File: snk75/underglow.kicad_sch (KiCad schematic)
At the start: 48 parts

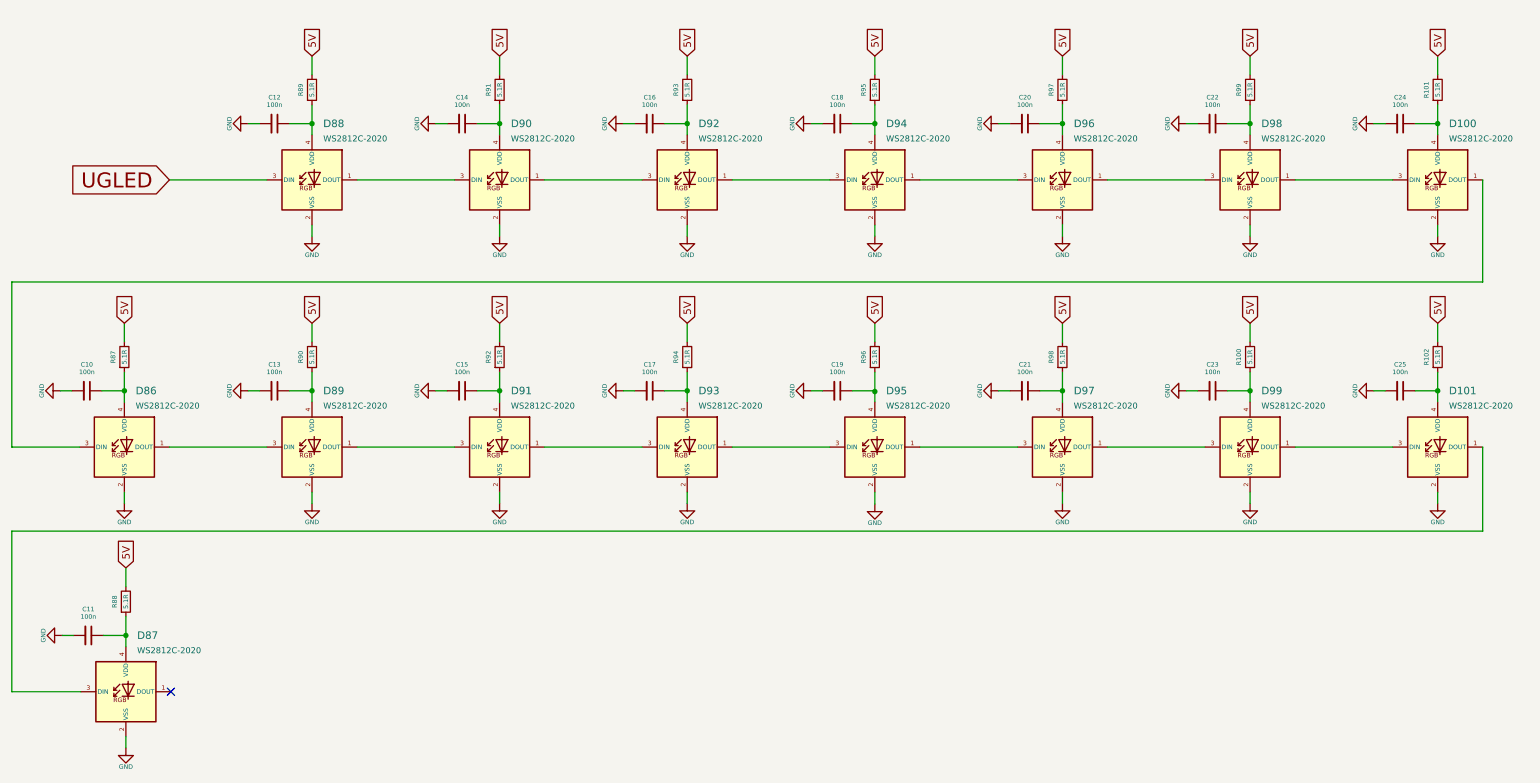
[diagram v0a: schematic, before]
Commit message: added components on board and began routing
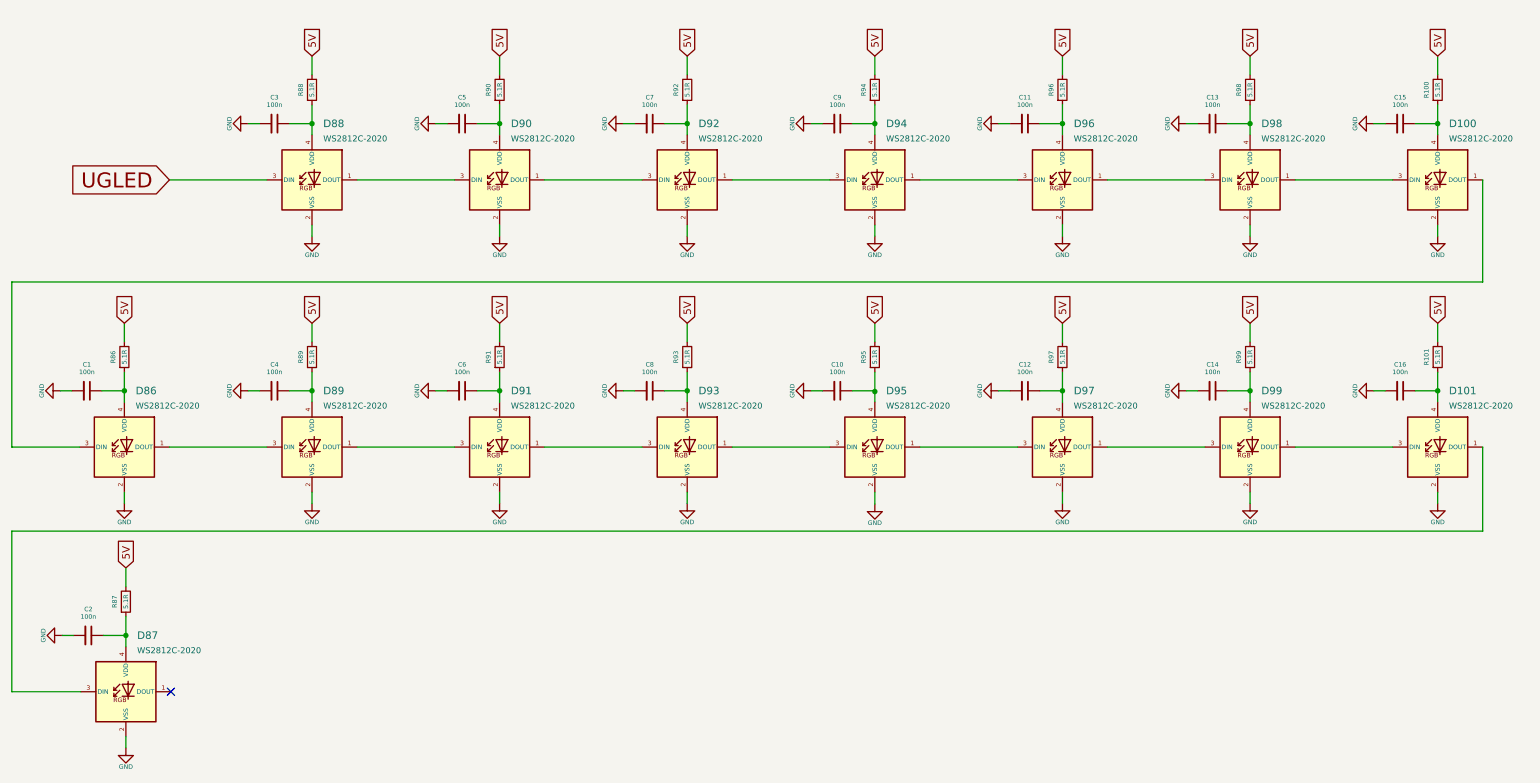
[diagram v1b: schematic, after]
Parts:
- renumbered C10 to C1, C19 to C10, C20 to C11, C21 to C12, C22 to C13, C23 to C14, C24 to C15, C25 to C16, C11 to C2, C12 to C3, C13 to C4, C14 to C5, C15 to C6, C16 to C7, C17 to C8, C18 to C9, R101 to R100, R102 to R101, R87 to R86, R88 to R87, R89 to R88, R90 to R89, R91 to R90, R92 to R91, R93 to R92, R94 to R93, R95 to R94, R96 to R95, R97 to R96, R98 to R97, R99 to R98, R100 to R99

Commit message: Nearly make all paths
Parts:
- C1, C10, C11, C12, C13, C14, C15, C16, C2, C3, C4, C5, C6, C7, C8, C9: value 100n -> 100nF; JLCPCB BOM (none) -> 1; LCSC (none) -> C1525; LCSC Part (none) -> C307331; LCSC Part Number (none) -> C307331
- D100, D101, D86, D87, D88, D89, D90, D91, D92, D93, D94, D95, D96, D97, D98, D99: JLCPCB BOM (none) -> 1; LCSC (none) -> C965556; LCSC Part (none) -> C965556; LCSC Part Number (none) -> C965556
- R100, R101, R86, R87, R88, R89, R90, R91, R92, R93, R94, R95, R96, R97, R98, R99: JLCPCB BOM (none) -> 1; LCSC (none) -> C25165; LCSC Part (none) -> C25165; LCSC Part Number (none) -> C25165
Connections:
- net at C10.1, R95.1: now also D95.4 (VDD)
- net 5V renamed +5V
